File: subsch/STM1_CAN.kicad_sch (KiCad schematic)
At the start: 17 parts

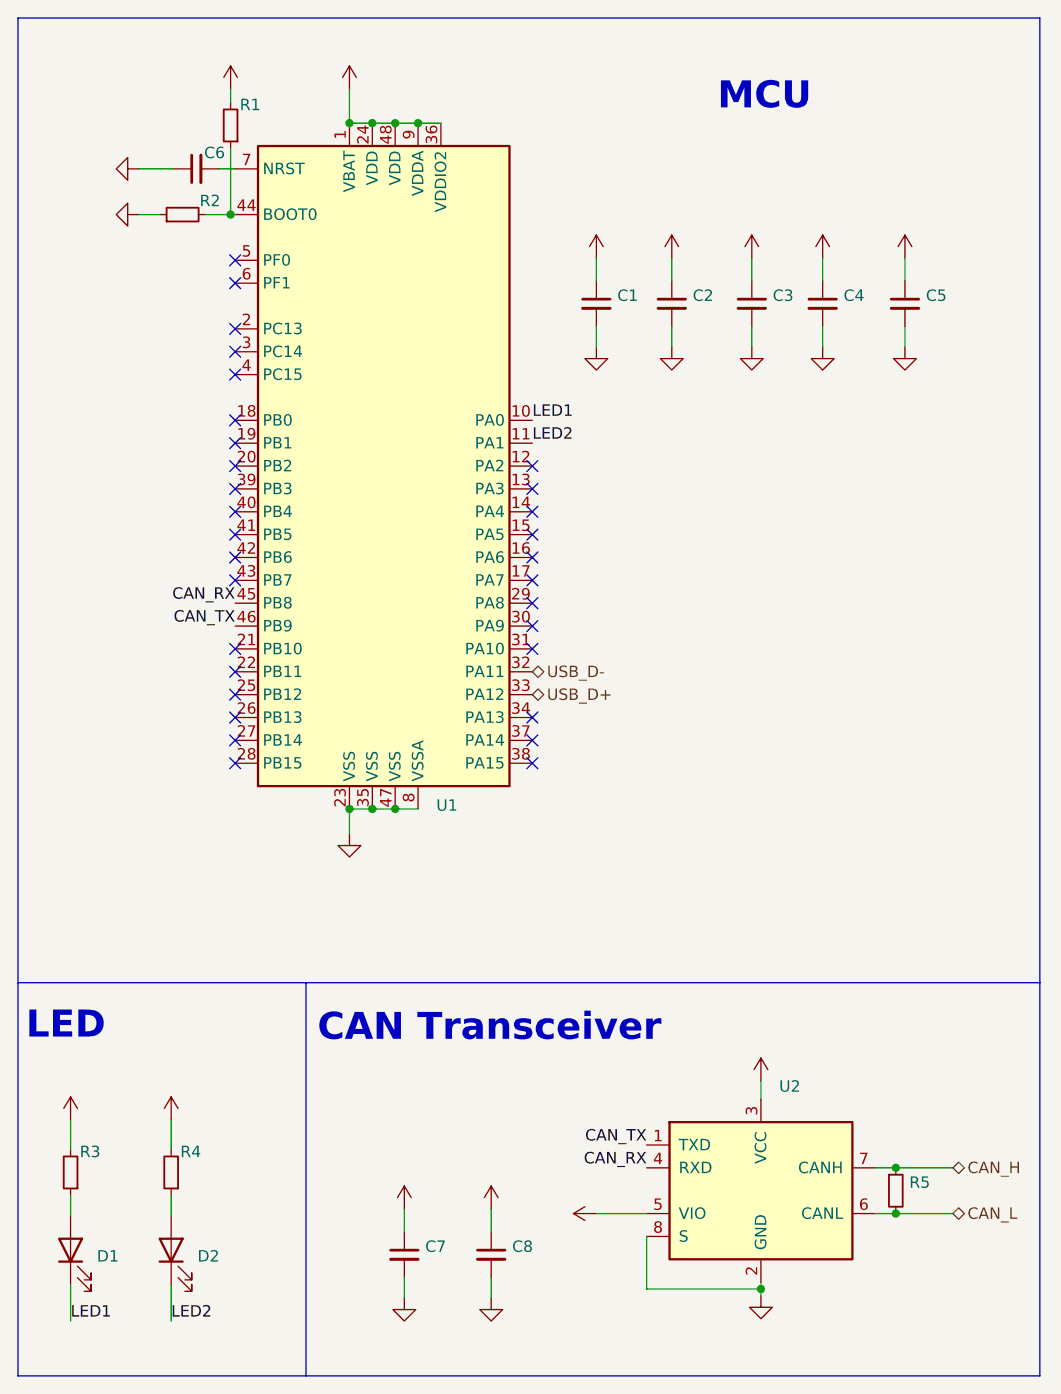
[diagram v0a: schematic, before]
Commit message: Big update on UART-pilot lamp/routings/connectors/esd protection
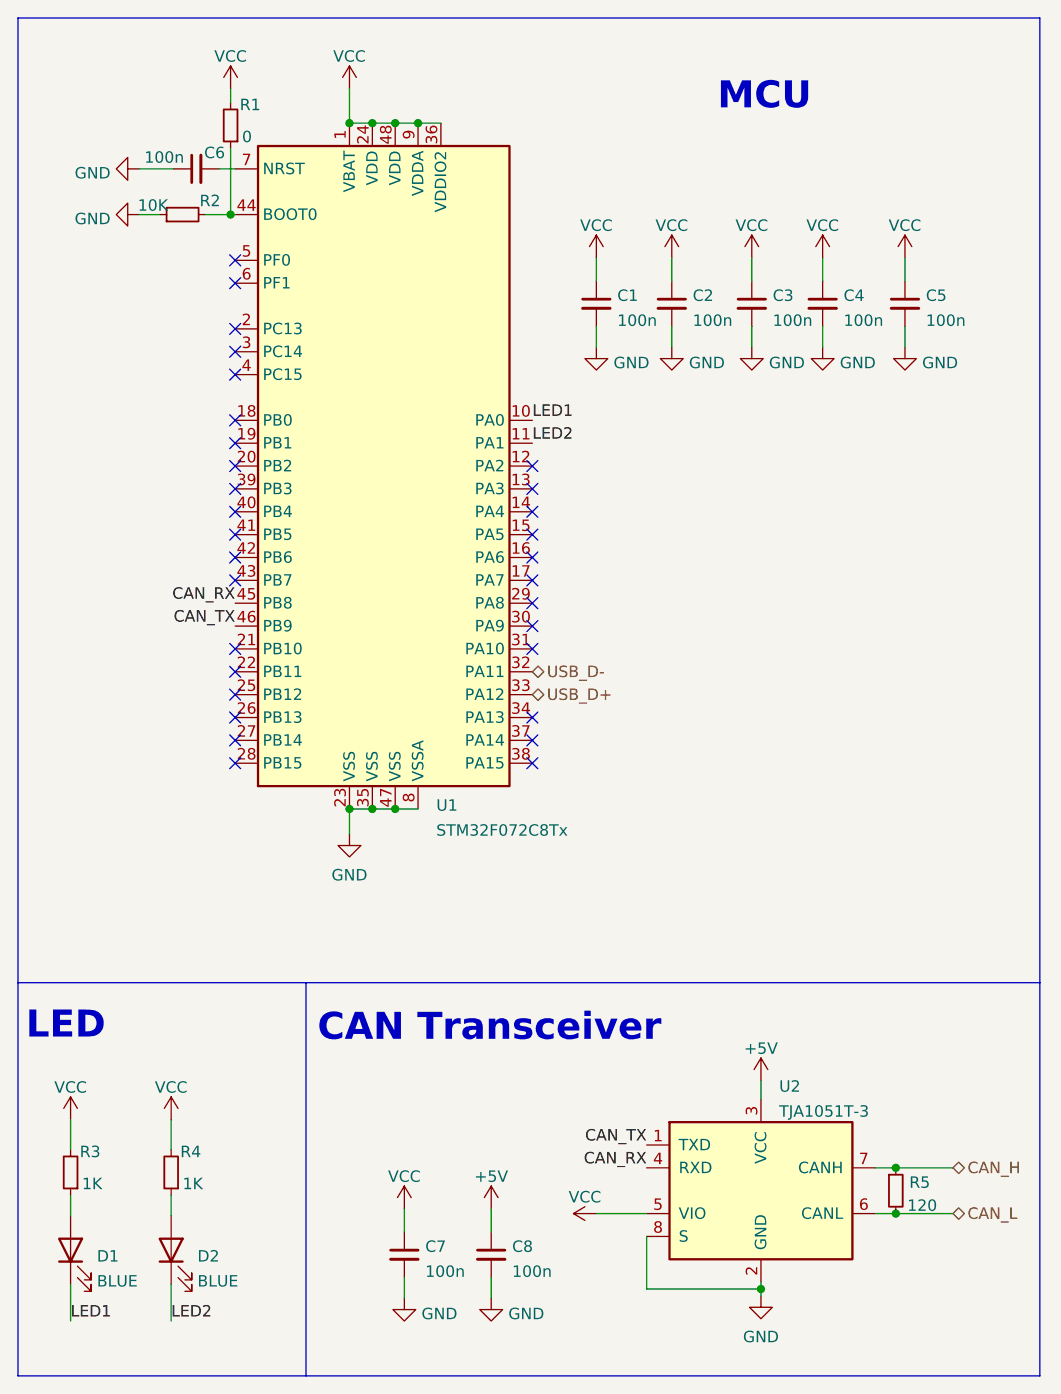
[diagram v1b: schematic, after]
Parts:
- C1, C2, C3, C4, C5, C6, C7, C8: value (none) -> 100n; footprint (none) -> Capacitor_SMD:C_0603_1608Metric
- D1, D2: value (none) -> BLUE; footprint (none) -> LED_SMD:LED_0603_1608Metric
- R1: value (none) -> 0; footprint (none) -> Resistor_SMD:R_0603_1608Metric
- R2: value (none) -> 10K; footprint (none) -> Resistor_SMD:R_0603_1608Metric
- R3, R4: value (none) -> 1K; footprint (none) -> Resistor_SMD:R_0603_1608Metric
- R5: value (none) -> 120; footprint (none) -> Resistor_SMD:R_0603_1608Metric
- U1: value (none) -> STM32F072C8Tx; footprint (none) -> Package_QFP:LQFP-48_7x7mm_P0.5mm
- U2: value (none) -> TJA1051T-3; footprint (none) -> Package_SO:SOIC-8_3.9x4.9mm_P1.27mm

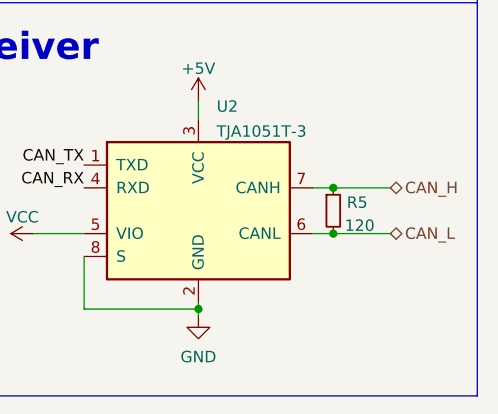
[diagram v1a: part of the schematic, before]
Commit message: Change connectors back to GH1.25&Add ESD for UART and CAN
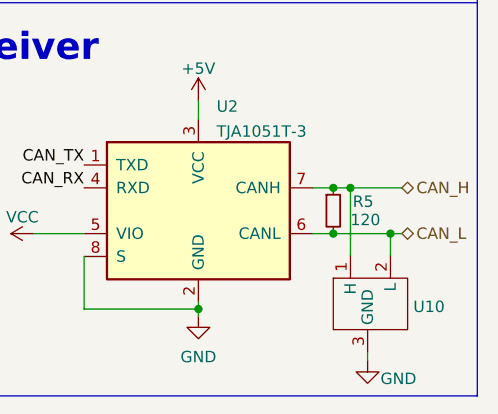
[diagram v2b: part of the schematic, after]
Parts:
- added U10: ~, Package_TO_SOT_SMD:SOT-23-3, symbol Extra IC:PESD1CAN
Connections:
- net CAN_H: now also U10.1 (H)
- net CAN_L: now also U10.2 (L)
- net GND: now also U10.3 (GND)
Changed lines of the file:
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@@
   (junction (at 70.104 112.014) (diameter 0) (color 0 0 0 0)
   )
+  (junction (at 134.62 156.972) (diameter 0) (color 0 0 0 0)
+  )
   (junction (at 128.27 151.892) (diameter 0) (color 0 0 0 0)
   )
@@
   )
   (junction (at 75.184 35.814) (diameter 0) (color 0 0 0 0)
+  )
+  (junction (at 130.175 151.892) (diameter 0) (color 0 0 0 0)
   )
   (junction (at 72.644 112.014) (diameter 0) (color 0 0 0 0)
@@
     (stroke (width 0) (type default))
   )
+  (wire (pts (xy 132.08 171.069) (xy 132.08 170.18))
+    (stroke (width 0) (type default))
+  )
   (wire (pts (xy 94.996 50.8) (xy 94.996 53.34))
     (stroke (width 0) (type default))
@@
     (stroke (width 0) (type default))
   )
+  (wire (pts (xy 134.62 156.972) (xy 135.89 156.972))
+    (stroke (width 0) (type default))
+  )
   (wire (pts (xy 125.984 151.892) (xy 128.27 151.892))
     (stroke (width 0) (type default))
@@
     (stroke (width 0) (type default))
   )
-  (wire (pts (xy 128.27 151.892) (xy 134.62 151.892))
+  (wire (pts (xy 128.27 151.892) (xy 130.175 151.892))
     (stroke (width 0) (type default))
   )
@@
     (stroke (width 0) (type default))
   )
+  (wire (pts (xy 130.175 151.892) (xy 135.89 151.892))
+    (stroke (width 0) (type default))
+  )
   (wire (pts (xy 113.284 164.592) (xy 113.284 165.354))
     (stroke (width 0) (type default))
@@
     (stroke (width 0) (type default))
   )
+  (wire (pts (xy 134.62 156.972) (xy 134.62 159.385))
+    (stroke (width 0) (type default))
+  )
   (wire (pts (xy 36.576 164.846) (xy 36.576 168.91))
     (stroke (width 0) (type default))
@@
   )
   (polyline (pts (xy 62.738 131.318) (xy 62.738 175.006))
+    (stroke (width 0) (type default))
+  )
+  (wire (pts (xy 130.175 151.892) (xy 130.175 159.385))
     (stroke (width 0) (type default))
   )
@@
     (effects (font (size 1.27 1.27)) (justify left))
   )
-  (hierarchical_label "CAN_L" (shape bidirectional) (at 134.62 156.972 0) (fields_autoplaced)
+  (hierarchical_label "CAN_L" (shape bidirectional) (at 135.89 156.972 0) (fields_autoplaced)
     (effects (font (size 1.27 1.27)) (justify left))
   )
-  (hierarchical_label "CAN_H" (shape bidirectional) (at 134.62 151.892 0) (fields_autoplaced)
+  (hierarchical_label "CAN_H" (shape bidirectional) (at 135.89 151.892 0) (fields_autoplaced)
     (effects (font (size 1.27 1.27)) (justify left))
   )
@@
   (symbol (lib_id "Device:R_Small") (at 128.27 154.432 0) (unit 1)
     (in_bom yes) (on_board yes) (dnp no)
-    (property "Reference" "R5" (at 129.7686 153.5235 0)
-      (effects (font (size 1.27 1.27)) (justify left))
-    )
-    (property "Value" "120" (at 129.54 156.083 0)
+    (property "Reference" "R5" (at 130.429 153.416 0)
+      (effects (font (size 1.27 1.27)) (justify left))
+    )
+    (property "Value" "120" (at 130.175 155.448 0)
       (effects (font (size 1.27 1.27)) (justify left))
     )
@@
         (path "/e63e39d7-6ac0-4ffd-8aa3-1841a4541b55/863ee6bd-9a8e-49fb-84d6-8d00fe76baf1"
           (reference "R5") (unit 1)
+        )
+      )
+    )
+  )
+  (symbol (lib_id "power:GND") (at 132.08 171.069 0) (unit 1)
+    (in_bom yes) (on_board yes) (dnp no)
+    (property "Reference" "#PWR085" (at 132.08 177.419 0)
+      (effects (font (size 1.27 1.27)) hide)
+    )
+    (property "Value" "GND" (at 135.509 173.101 0)
+      (effects (font (size 1.27 1.27)))
+    )
+    (property "Footprint" "" (at 132.08 171.069 0)
+      (effects (font (size 1.27 1.27)) hide)
+    )
+    (property "Datasheet" "" (at 132.08 171.069 0)
+      (effects (font (size 1.27 1.27)) hide)
+    )
+    (pin "1")
+    (instances
+      (project "USB2XXX"
+        (path "/e63e39d7-6ac0-4ffd-8aa3-1841a4541b55/863ee6bd-9a8e-49fb-84d6-8d00fe76baf1"
+          (reference "#PWR085") (unit 1)
         )
       )
@@
         )
       )
+    )
+  )
+  (symbol (lib_id "Extra IC:PESD1CAN") (at 132.715 165.735 0) (unit 1)
+    (in_bom yes) (on_board yes) (dnp no) (fields_autoplaced)
+    (property "Reference" "U10" (at 137.16 165.0993 0)
+      (effects (font (size 1.27 1.27)) (justify left))
+    )
+    (property "Value" "~" (at 131.445 159.385 0)
+      (effects (font (size 1.27 1.27)))
+    )
+    (property "Footprint" "Package_TO_SOT_SMD:SOT-23-3" (at 131.445 159.385 0)
+      (effects (font (size 1.27 1.27)) hide)
+    )
+    (property "Datasheet" "" (at 131.445 159.385 0)
+      (effects (font (size 1.27 1.27)) hide)
+    )
+    (pin "1")
+    (pin "2")
+    (pin "3")
+    (instances
+      (project "USB2XXX"
+        (path "/e63e39d7-6ac0-4ffd-8aa3-1841a4541b55/863ee6bd-9a8e-49fb-84d6-8d00fe76baf1"
+          (reference "U10") (unit 1)
+        )
+      )

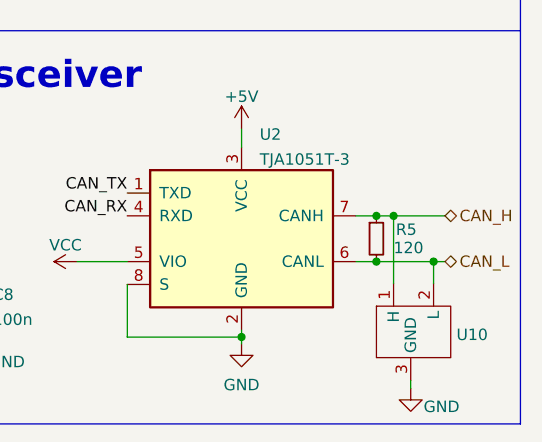
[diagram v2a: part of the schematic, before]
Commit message: Adaption for SMT(hotfix)
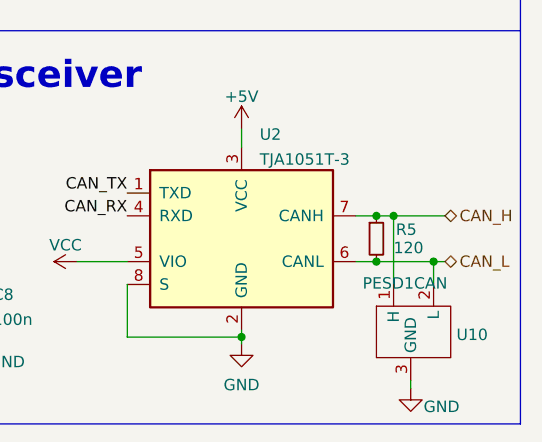
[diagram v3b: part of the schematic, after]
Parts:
- U10: value ~ -> PESD1CAN
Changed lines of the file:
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@@
       (effects (font (size 1.27 1.27)) (justify left))
     )
-    (property "Value" "~" (at 131.445 159.385 0)
+    (property "Value" "PESD1CAN" (at 131.445 159.385 0)
       (effects (font (size 1.27 1.27)))
     )
